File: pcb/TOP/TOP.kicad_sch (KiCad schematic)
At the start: 65 parts, among them J1 Conn_01x04

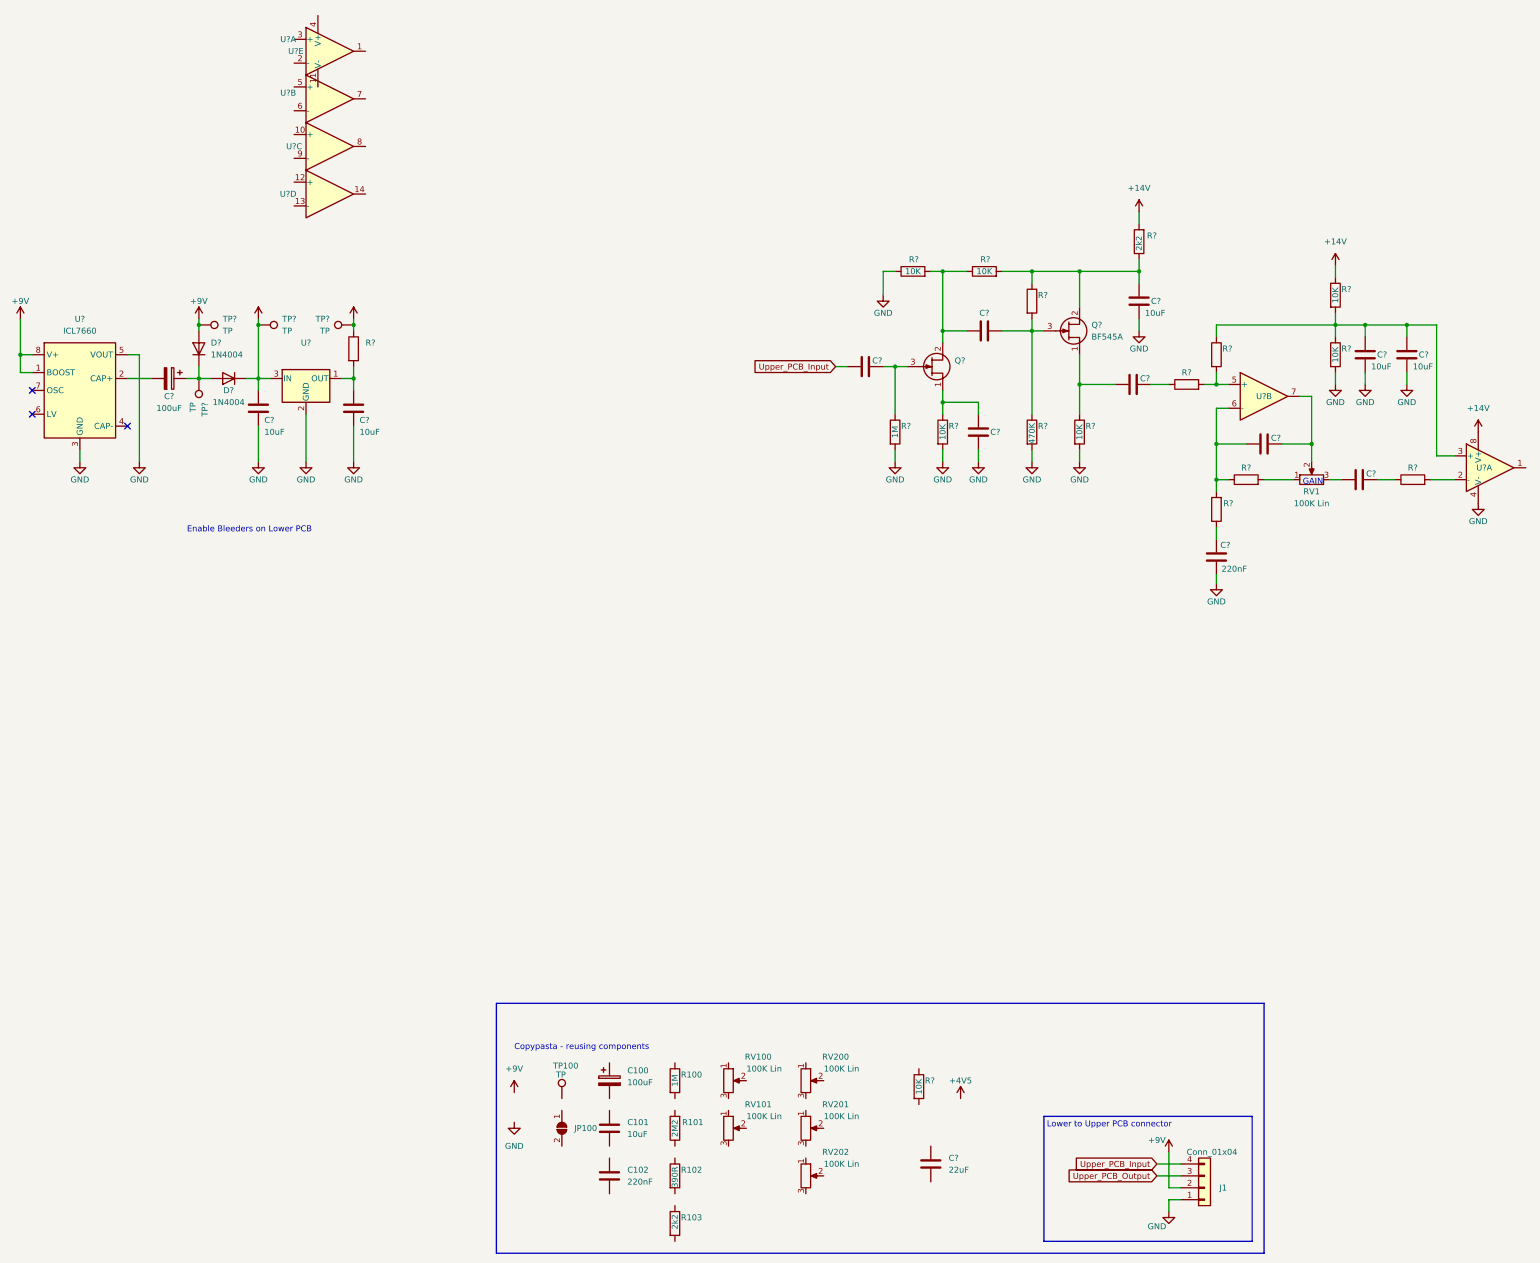
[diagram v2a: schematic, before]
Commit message: [All] Flip board to board connector on upper PCB (obstructed some silk)
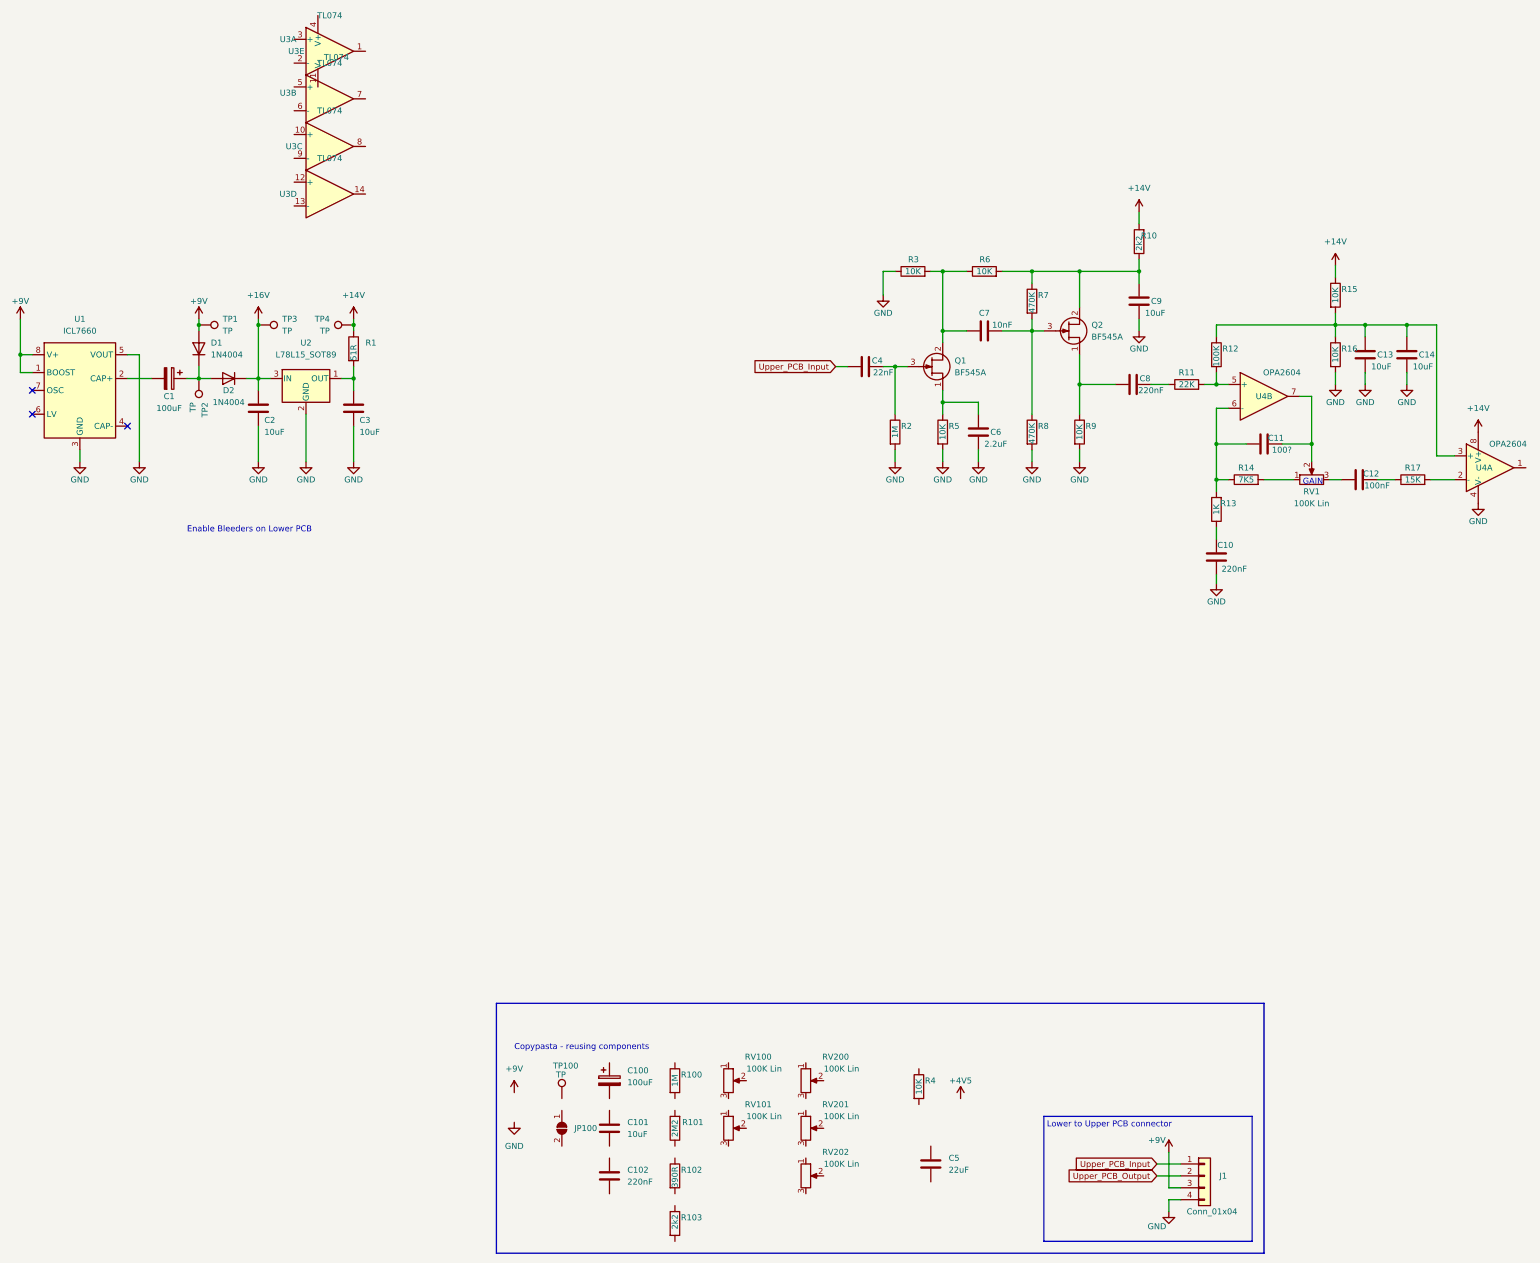
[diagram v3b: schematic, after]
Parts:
- C11: renamed from C?; value (none) -> 100?
- C12: renamed from C?; value (none) -> 100nF
- C4: renamed from C?; value (none) -> 22nF
- C6: renamed from C?; value (none) -> 2.2uF
- C7: renamed from C?; value (none) -> 10nF
- C8: renamed from C?; value (none) -> 220nF
- Q1: renamed from Q?; value (none) -> BF545A; footprint (none) -> Package_TO_SOT_SMD:SOT-23
- R1: renamed from R?; value (none) -> 51R
- R11: renamed from R?; value (none) -> 22K
- R12: renamed from R?; value (none) -> 100K
- R13: renamed from R?; value (none) -> 1K
- R14: renamed from R?; value (none) -> 7K5
- R17: renamed from R?; value (none) -> 15K
- R7: renamed from R?; value (none) -> 470K
- U2: renamed from U?; value (none) -> L78L15_SOT89; footprint (none) -> Package_TO_SOT_SMD:SOT-89-3
- U3: renamed from U?; value (none) -> TL074
- U4: renamed from U?; value (none) -> OPA2604
- gave numbers to parts that had none: 26
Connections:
- net +9V: now also J1.3 (Pin_3); no longer J1.2 (Pin_2)
- net GND: now also J1.4 (Pin_4); no longer J1.1 (Pin_1)
- net Upper_PCB_Input: now also J1.1 (Pin_1); no longer J1.4 (Pin_4)
- net Upper_PCB_Output: now also J1.2 (Pin_2); no longer J1.3 (Pin_3)

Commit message: [TOP] Continue schematic
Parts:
- removed C5: 22uF, Capacitor_SMD:C_1206_3216Metric, symbol Device:C
- removed R100: 1M, Resistor_SMD:R_0603_1608Metric, symbol Device:R
- removed R101: 2M2, Resistor_SMD:R_0603_1608Metric, symbol Device:R
- removed R102: 390R, Resistor_SMD:R_0603_1608Metric, symbol Device:R
- removed R103: 2k2, Resistor_SMD:R_0603_1608Metric, symbol Device:R
- removed R4: 10K, Resistor_SMD:R_0603_1608Metric, symbol Device:R
- added C? (x12): (no value), symbol Device:C
- added C?: 22nF, symbol Device:C
- added C?: 220nF, symbol Device:C
- added R? (x3): (no value), Resistor_SMD:R_0603_1608Metric, symbol Device:R
- added R? (x6): (no value), symbol Device:R
- added R? (x8): 10K, Resistor_SMD:R_0603_1608Metric, symbol Device:R
- added R?: 1M, Resistor_SMD:R_0603_1608Metric, symbol Device:R
- added R?: 1K, Resistor_SMD:R_0603_1608Metric, symbol Device:R
- added R?: 47K, symbol Device:R
- RV100, RV101, RV200, RV201, RV202: value 100K Lin -> (none)
- U3: value TL074 -> (none)
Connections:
- net +4V5: now also U3.4 (V+), R?.1
- net GND: now also RV100.3, U3.11 (V-), C?.1, C?.1, C?.2, R?.1, R?.2
- net Upper_PCB_Output: now also C?.1
- net at R17.2, U4.2 (-): now also C?.2, R?.1
- net at U3.10 (+): now also C?.1, R?.1
- net at U3.8: now also U3.9 (-), R?.2
- net at RV201.1: now also RV200.1, U3.12 (+), R?.2, R?.2
- net at RV201.2: now also C?.2
- net at RV201.3: now also RV200.3, U3.13 (-), C?.2, R?.1, R?.1
- net at U3.5 (+): now also C?.1, R?.2
- net at U3.6 (-): now also U3.7, R?.2
- net at U4.1: now also C?.1, C?.2, C?.2, R?.2
- net at U3.14: now also C?.1, C?.2, R?.2
- net at U3.1: now also U3.2 (-), R?.1
- net at U3.3 (+): now also R?.2, R?.2
- net at RV202.1: now also R?.1
- net at RV202.2: now also C?.2
- net at RV202.3: now also R?.2
- net at RV100.1: now also R?.1, R?.2
- net at RV100.2: now also C?.2
- net at RV101.1: now also R?.1
- net at RV101.2: now also RV101.3, C?.1, R?.1, R?.1, R?.2, R?.2
- net at RV200.2: now also C?.1
- new net: C?.2, R?.1, R?.1
- new net: C?.1, R?.2
- new net: C?.2, R?.1, R?.2
- new net: R?.1, R?.2, R?.2
- new net: C?.1, C?.2, R?.1
- new net: C?.2, R?.2 (x2)
- new net: C?.1, R?.1 (x3)
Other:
- note added: "Bass"
- note added: "Mid"
- note added: "MidR"
- note added: "Treb"
- note added: "Vol"
- moved on the sheet: C1, C10, C11, C12, C13, C14, C2, C3, C4, C6, C7, C8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

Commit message: [TOP] Finish initial work on schematic
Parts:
- removed C100: 100uF, Capacitor_THT:CP_Radial_D5.0mm_P2.00mm, symbol Device:C_Polarized
- removed C101: 10uF, Capacitor_SMD:C_0805_2012Metric, symbol Device:C
- removed C102: 220nF, Capacitor_SMD:C_0603_1608Metric, symbol Device:C
- removed C?: (no value), symbol Device:C
- removed JP100: Jmp, Jumper:SolderJumper-2_P1.3mm_Open_TrianglePad1.0x1.5mm, symbol Jumper:SolderJumper_2_Open
- removed TP100: TP, TestPoint:TestPoint_Pad_D2.0mm, symbol Connector:TestPoint
- added C20, C22: (no value), symbol Device:C
- added JP_VOut_GND1: (no value), symbol Jumper:SolderJumper_2_Open
- added TP_14V_B1, TP_16V_B1, TP_GND1, TP_Gain1, TP_Inp1: (no value), symbol Connector:TestPoint
- C1: value 100uF -> (none); footprint Capacitor_THT:CP_Radial_D5.0mm_P2.00mm -> (none); LCSC C108360 -> C15850
- C10, C8: value 220nF -> (none)
- C11: value 100? -> (none)
- C12: value 100nF -> (none)
- C13, C14, C2, C3, C9: value 10uF -> (none); footprint Capacitor_SMD:C_0805_2012Metric -> (none)
- C16: renamed from C?; value 220nF -> (none)
- C23: renamed from C?; value 22nF -> (none)
- C4: value 22nF -> (none)
- C6: value 2.2uF -> (none)
- C7: value 10nF -> (none)
- D1, D2: value 1N4004 -> (none); footprint Diode_THT:D_DO-41_SOD81_P10.16mm_Horizontal -> (none)
- J1: value Conn_01x04 -> (none); footprint Connector_JST:JST_XH_B4B-XH-A_1x04_P2.50mm_Vertical -> (none)
- Q1, Q2: value BF545A -> (none); footprint Package_TO_SOT_SMD:SOT-23 -> (none)
- R1: value 51R -> (none)
- R10: value 2k2 -> (none); footprint Resistor_SMD:R_0603_1608Metric -> (none)
- R11: value 22K -> (none)
- R12: value 100K -> (none)
- R13: value 1K -> (none)
- R14: value 7K5 -> (none)
- R15, R16, R3, R5, R6, R9: value 10K -> (none); footprint Resistor_SMD:R_0603_1608Metric -> (none)
- R17: value 15K -> (none)
- R18, R25, R26, R27, R31, R33, R36: renamed from R?; value 10K -> (none); footprint Resistor_SMD:R_0603_1608Metric -> (none)
- R2: value 1M -> (none); footprint Resistor_SMD:R_0603_1608Metric -> (none)
- R20: renamed from R?; value 10K -> (none); footprint Resistor_SMD:R_0603_1608Metric -> (none); LCSC C25804 -> (none)
- R21: renamed from R?; value 47K -> (none)
- R24: renamed from R?; value 1M -> (none); footprint Resistor_SMD:R_0603_1608Metric -> (none)
- R30, R35: renamed from R?; footprint Resistor_SMD:R_0603_1608Metric -> (none)
- R32: renamed from R?; value 1K -> (none); footprint Resistor_SMD:R_0603_1608Metric -> (none)
- R4: renamed from R?; footprint Resistor_SMD:R_0603_1608Metric -> (none); LCSC C25804 -> (none)
- R7, R8: value 470K -> (none)
- RV1: value 100K Lin -> (none); footprint Potentiometer_THT:Potentiometer_Alpha_RD901F-40-00D_Single_Vertical -> (none)
- RV100, RV101, RV200, RV201, RV202: footprint Potentiometer_THT:Potentiometer_Alpha_RD901F-40-00D_Single_Vertical -> (none)
- TP_14V1: renamed from TP4; value TP -> (none); footprint TestPoint:TestPoint_Pad_D2.0mm -> (none)
- TP_16V1: renamed from TP3; value TP -> (none); footprint TestPoint:TestPoint_Pad_D2.0mm -> (none)
- TP_9V1: renamed from TP1; value TP -> (none); footprint TestPoint:TestPoint_Pad_D2.0mm -> (none)
- TP_DD1: renamed from TP2; value TP -> (none); footprint TestPoint:TestPoint_Pad_D2.0mm -> (none)
- U1: value ICL7660 -> (none)
- U2: value L78L15_SOT89 -> (none); footprint Package_TO_SOT_SMD:SOT-89-3 -> (none)
- U4: value OPA2604 -> (none)
- gave numbers to parts that had none: 17
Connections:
- net GND: now also C20.2, C22.2, JP_VOut_GND1.2 (B), TP_GND1.1; no longer U1.5 (VOUT)
- net at R24.1, R25.2, R26.1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: now also C20.1, C22.1, TP_16V_B1.1
- net at C13.1, C14.1, R12.1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: now also TP_14V_B1.1
- net at C8.2, Q2.1 (S), R9.1: now also TP_Inp1.1
- net at C19.2, RV100.2: now also TP_Gain1.1
- new net: JP_VOut_GND1.1 (A), U1.5 (VOUT)
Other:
- note added: "Voltage doubler"
- note removed: "Copypasta - reusing components"
- title: PedalDev_UpperRaw -> PedalDev_TOP
- moved on the sheet: C1, C10, C11, C12, C13, C14, C15, C16, C17, C18, C19, C2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

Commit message: [TOP] BOM consolidation
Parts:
- added C29: (no value), symbol Device:C
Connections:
- net GND: now also C18.2, C29.2; no longer C18.1
- net at R22.2: now also C18.1, C29.1; no longer C18.2
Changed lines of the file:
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@@
   (junction (at 170.18 112.395) (diameter 0) (color 0 0 0 0)
   )
+  (junction (at 220.98 177.8) (diameter 0) (color 0 0 0 0)
+  )
   (junction (at 208.28 106.045) (diameter 0) (color 0 0 0 0)
   )
@@
     (stroke (width 0) (type default) (color 0 0 0 0))
   )
-  (wire (pts (xy 220.98 185.42) (xy 220.98 189.23))
+  (wire (pts (xy 220.98 187.96) (xy 220.98 189.23))
     (stroke (width 0) (type default) (color 0 0 0 0))
   )
@@
     (stroke (width 0) (type default) (color 0 0 0 0))
   )
+  (wire (pts (xy 220.98 177.8) (xy 220.98 180.34))
+    (stroke (width 0) (type default) (color 0 0 0 0))
+  )
   (wire (pts (xy 285.75 179.07) (xy 294.64 179.07))
     (stroke (width 0) (type default) (color 0 0 0 0))
@@
     (stroke (width 0) (type default) (color 0 0 0 0))
   )
+  (wire (pts (xy 213.36 177.8) (xy 220.98 177.8))
+    (stroke (width 0) (type default) (color 0 0 0 0))
+  )
   (wire (pts (xy 326.39 118.11) (xy 328.93 118.11))
     (stroke (width 0) (type default) (color 0 0 0 0))
@@
     (stroke (width 0) (type default) (color 0 0 0 0))
   )
+  (wire (pts (xy 213.36 180.34) (xy 213.36 177.8))
+    (stroke (width 0) (type default) (color 0 0 0 0))
+  )
+  (wire (pts (xy 213.36 187.96) (xy 213.36 189.23))
+    (stroke (width 0) (type default) (color 0 0 0 0))
+  )
   (wire (pts (xy 44.45 160.02) (xy 44.45 162.56))
     (stroke (width 0) (type default) (color 0 0 0 0))
@@
     (pin "4")
   )
+  (symbol (lib_id "power:GND") (at 213.36 189.23 0) (unit 1)
+    (in_bom yes) (on_board yes)
+    (property "Reference" "#PWR0118" (id 0) (at 213.36 195.58 0)
+      (effects (font (size 1.27 1.27)) hide)
+    )
+    (property "Value" "GND" (id 1) (at 213.36 193.04 0))
+    (property "Footprint" "" (id 2) (at 213.36 189.23 0)
+      (effects (font (size 1.27 1.27)) hide)
+    )
+    (property "Datasheet" "" (id 3) (at 213.36 189.23 0)
+      (effects (font (size 1.27 1.27)) hide)
+    )
+    (pin "1")
+  )
   (symbol (lib_id "Transistor_FET:BF545A") (at 77.47 134.62 0) (unit 1)
     (in_bom yes) (on_board yes)
@@
   (symbol (lib_id "Device:C") (at 238.76 176.53 270) (unit 1)
     (in_bom yes) (on_board yes)
-    (property "Reference" "C19" (id 0) (at 241.3 175.26 90))
+    (property "Reference" "C19" (id 0) (at 242.57 175.26 90))
     (property "Value" "" (id 1) (at 238.76 180.34 90))
     (property "Footprint" "" (id 2) (at 234.95 177.4952 0)
@@
     (pin "2")
   )
+  (symbol (lib_id "Device:C") (at 220.98 184.15 0) (unit 1)
+    (in_bom yes) (on_board yes)
+    (property "Reference" "C29" (id 0) (at 223.52 181.61 0))
+    (property "Value" "" (id 1) (at 223.52 186.69 0))
+    (property "Footprint" "" (id 2) (at 221.9452 187.96 0)
+      (effects (font (size 1.27 1.27)) hide)
+    )
+    (property "Datasheet" "~" (id 3) (at 220.98 184.15 0)
+      (effects (font (size 1.27 1.27)) hide)
+    )
+    (pin "1")
+    (pin "2")
+  )
   (symbol (lib_id "power:GND") (at 104.14 188.595 0) (unit 1)
     (in_bom yes) (on_board yes)
@@
     (pin "1")
   )
+  (symbol (lib_id "Device:C") (at 213.36 184.15 0) (unit 1)
+    (in_bom yes) (on_board yes)
+    (property "Reference" "C18" (id 0) (at 215.9 181.61 0))
+    (property "Value" "" (id 1) (at 215.9 186.69 0))
+    (property "Footprint" "" (id 2) (at 214.3252 187.96 0)
+      (effects (font (size 1.27 1.27)) hide)
+    )
+    (property "Datasheet" "~" (id 3) (at 213.36 184.15 0)
+      (effects (font (size 1.27 1.27)) hide)
+    )
+    (pin "1")
+    (pin "2")
+  )
   (symbol (lib_id "Connector:TestPoint") (at 295.91 95.25 0) (unit 1)
     (in_bom no) (on_board yes)
@@
     (pin "2")
   )
-  (symbol (lib_id "Device:C") (at 220.98 181.61 180) (unit 1)
-    (in_bom yes) (on_board yes)
-    (property "Reference" "C18" (id 0) (at 218.44 179.07 0))
-    (property "Value" "" (id 1) (at 217.805 184.15 0))
-    (property "Footprint" "" (id 2) (at 220.0148 177.8 0)
-      (effects (font (size 1.27 1.27)) hide)
-    )
-    (property "Datasheet" "~" (id 3) (at 220.98 181.61 0)
-      (effects (font (size 1.27 1.27)) hide)
-    )
-    (pin "1")
-    (pin "2")
-  )
   (symbol (lib_id "Device:C") (at 179.07 163.83 270) (unit 1)
     (in_bom yes) (on_board yes)
@@
       (reference "#PWR0117") (unit 1) (value "GND") (footprint "")
     )
+    (path "/317bec43-b8c6-43cb-a341-442fe020632c"
+      (reference "#PWR0118") (unit 1) (value "GND") (footprint "")
+    )
     (path "/084627ff-e2be-428d-9154-b26a0a9a72db"
       (reference "#PWR0119") (unit 1) (value "+14V") (footprint "")
@@
     )
     (path "/d955d937-8643-495e-ab11-0c0a4167292a"
-      (reference "C17") (unit 1) (value "51nF") (footprint "")
+      (reference "C17") (unit 1) (value "47nF") (footprint "")
     )
-    (path "/e359ffad-a4d8-4c96-95e1-e095287476ee"
-      (reference "C18") (unit 1) (value "2.2nF") (footprint "")
+    (path "/d467cd27-f907-49c8-bb89-d0ed7c11fe32"
+      (reference "C18") (unit 1) (value "1nF") (footprint "")
     )
     (path "/417d1c04-24e7-4ab5-bc08-e1453d4024bc"
@@
       (reference "C28") (unit 1) (value "680nF") (footprint "")
     )
+    (path "/8d94cc0e-e2e1-4ec5-bb2c-e540dc18d37e"
+      (reference "C29") (unit 1) (value "1nF") (footprint "")
+    )
     (path "/0ff4343c-407d-4c6b-92a4-beb371940202"
       (reference "D1") (unit 1) (value "1N4004") (footprint "")
@@
     )
     (path "/6a0eb4f3-0fe9-4ffb-bb49-5e64936123e6"
-      (reference "R10") (unit 1) (value "2k2") (footprint "Resistor_SMD:R_0603_1608Metric")
+      (reference "R10") (unit 1) (value "2K2") (footprint "Resistor_SMD:R_0603_1608Metric")
     )
     (path "/a2b19378-f7a1-4017-9603-c2dbb7448610"

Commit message: [TOP] Assign footprints and LCSC part numbers
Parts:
- C10, C16, C25, C8: LCSC (none) -> C21120
- C11: LCSC (none) -> C14858
- C12: LCSC (none) -> C14663
- C15, C7: LCSC (none) -> C1710
- C17: LCSC (none) -> C1622
- C18, C27, C29: LCSC (none) -> C1588
- C19, C28: LCSC (none) -> C1623
- C21, C23, C24, C4: LCSC (none) -> C21122
- C26: LCSC (none) -> C31658
- C5: LCSC (none) -> C1620
- C6: LCSC (none) -> C23630
- D1, D2: LCSC (none) -> C433394
- R1: LCSC (none) -> C23197
- R10, R28: LCSC (none) -> C4190
- R11: LCSC (none) -> C31850
- R12: LCSC (none) -> C25803
- R13, R23, R32: LCSC (none) -> C21190
- R14, R29: LCSC (none) -> C23234
- R17: LCSC (none) -> C22809
- R19, R20, R21: LCSC (none) -> C25819
- R2, R24, R4: LCSC (none) -> C22935
- R22: LCSC (none) -> C23153
- R30: LCSC (none) -> C23179
- R34: LCSC (none) -> C23138
- R35, R7, R8: LCSC (none) -> C23178
- U1: LCSC (none) -> C356724
- U2: LCSC (none) -> C411742
- U3: LCSC (none) -> C6963
- U4: LCSC (none) -> C30608
